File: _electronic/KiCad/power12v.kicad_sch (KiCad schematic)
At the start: 14 parts

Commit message: external flashing header
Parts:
- J_POW1: footprint Connector_BarrelJack:BarrelJack_GCT_DCJ200-10-A_Horizontal -> SnapEDA Library:BarrelJack_GCT_DCJ200-10-A_Horizontal
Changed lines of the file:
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@@
       (effects (font (size 1.27 1.27)) hide)
     )
-    (property "Footprint" "Connector_BarrelJack:BarrelJack_GCT_DCJ200-10-A_Horizontal" (id 2) (at 90.17 89.916 0)
+    (property "Footprint" "SnapEDA Library:BarrelJack_GCT_DCJ200-10-A_Horizontal" (id 2) (at 90.17 89.916 0)
       (effects (font (size 1.27 1.27)) hide)
     )

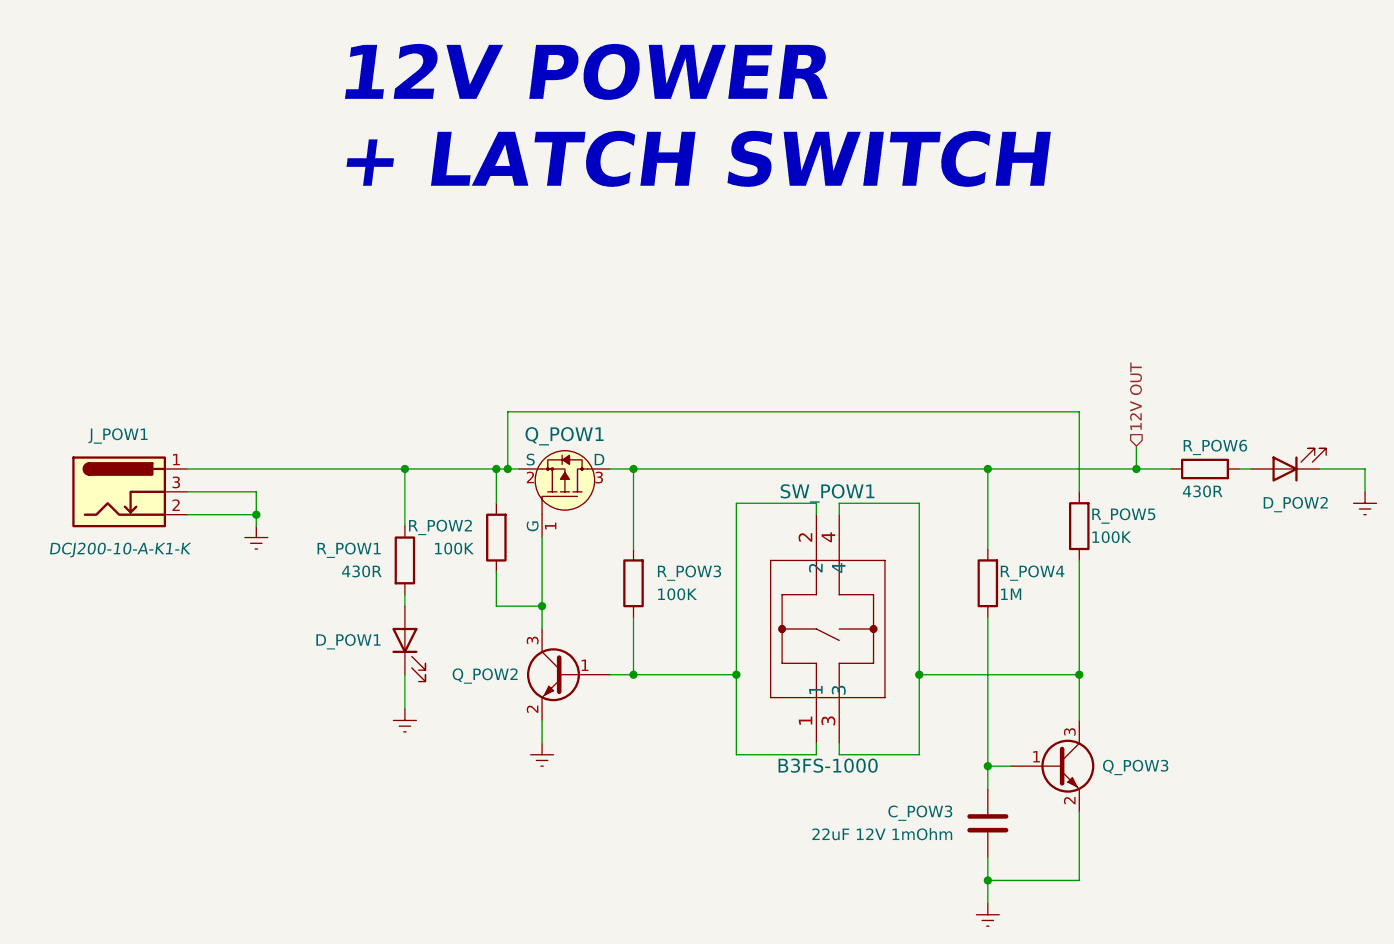
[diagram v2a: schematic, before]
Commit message: 6v and power latch backup
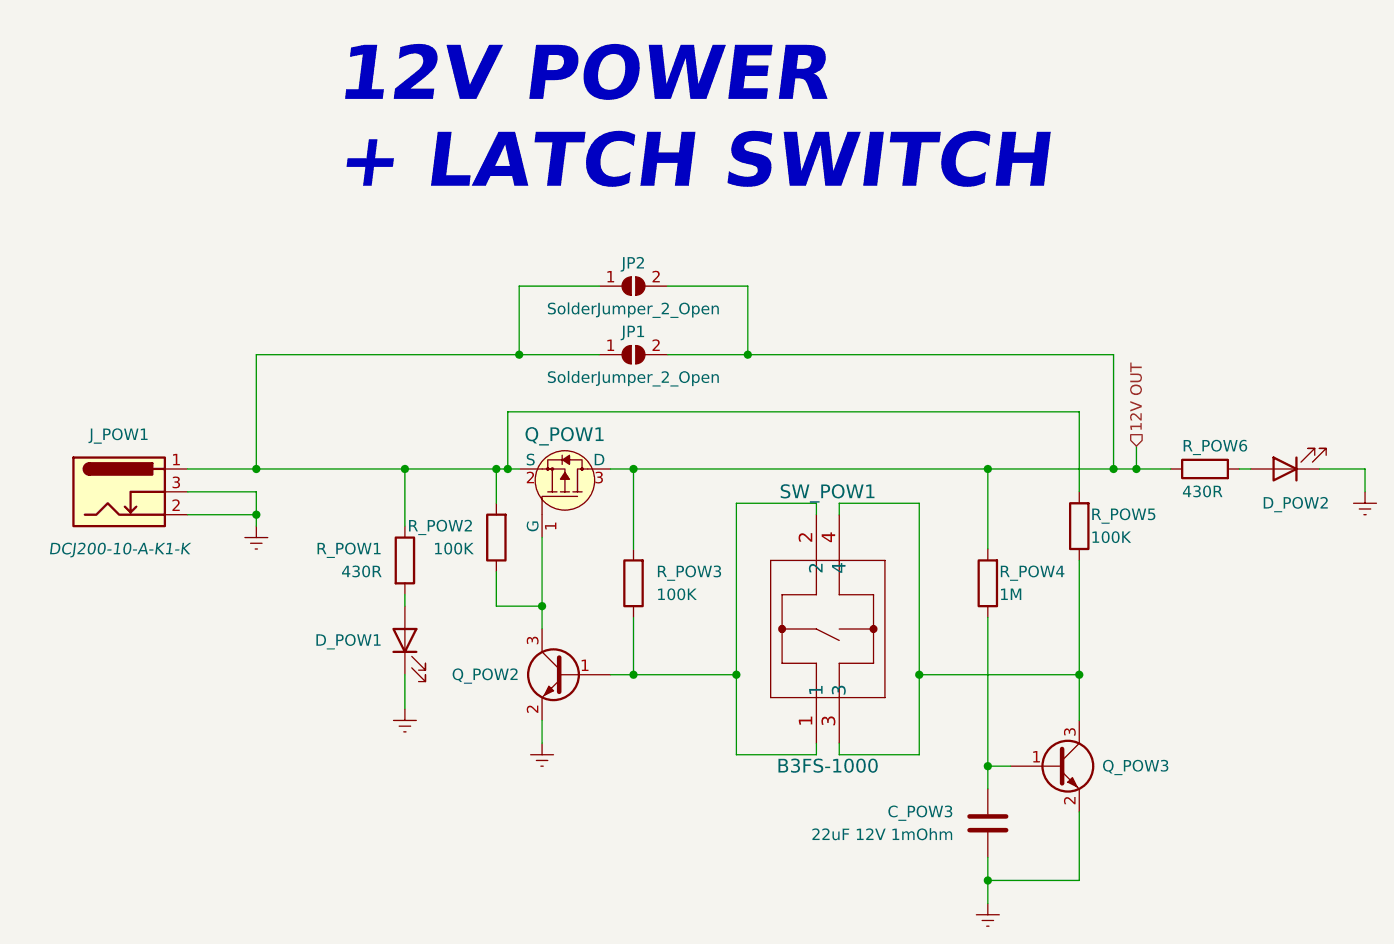
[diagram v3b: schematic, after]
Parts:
- added JP1, JP2: SolderJumper_2_Open, Jumper:SolderJumper-2_P1.3mm_Open_Pad1.0x1.5mm, symbol Jumper:SolderJumper_2_Open
- Q_POW1: value IRLML6302TRPBF -> SQ2351ES-T1_GE3; # IRLML6302TRPBF -> SQ2351ES-T1_GE3; Obs wes SI2303CDS-T1-BE3 ?? Id - Continuous Drain Current -> (none)
- Q_POW2, Q_POW3: Obs wes -> (none)
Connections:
- net 12V OUT: now also JP1.2 (B), JP2.2 (B)
- net at J_POW1.1, Q_POW1.2 (S), R_POW1.1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: now also JP1.1 (A), JP2.1 (A)
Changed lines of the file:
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@@
   (junction (at 201.93 86.36) (diameter 0) (color 0 0 0 0)
   )
+  (junction (at 158.75 73.66) (diameter 0) (color 0 0 0 0)
+  )
   (junction (at 130.81 86.36) (diameter 0) (color 0 0 0 0)
   )
+  (junction (at 104.14 86.36) (diameter 0) (color 0 0 0 0)
+  )
   (junction (at 120.65 86.36) (diameter 0) (color 0 0 0 0)
   )
@@
   (junction (at 195.58 109.22) (diameter 0) (color 0 0 0 0)
   )
+  (junction (at 199.39 86.36) (diameter 0) (color 0 0 0 0)
+  )
   (junction (at 132.08 86.36) (diameter 0) (color 0 0 0 0)
   )
@@
   (junction (at 185.42 132.08) (diameter 0) (color 0 0 0 0)
   )
+  (junction (at 133.35 73.66) (diameter 0) (color 0 0 0 0)
+  )
   (junction (at 185.42 86.36) (diameter 0) (color 0 0 0 0)
   )
@@
     (stroke (width 0) (type default) (color 0 0 0 0))
   )
+  (wire (pts (xy 158.75 66.04) (xy 158.75 73.66))
+    (stroke (width 0) (type default) (color 0 0 0 0))
+  )
+  (wire (pts (xy 158.75 73.66) (xy 199.39 73.66))
+    (stroke (width 0) (type default) (color 0 0 0 0))
+  )
+  (wire (pts (xy 104.14 86.36) (xy 120.65 86.36))
+    (stroke (width 0) (type default) (color 0 0 0 0))
+  )
   (wire (pts (xy 130.81 86.36) (xy 132.08 86.36))
     (stroke (width 0) (type default) (color 0 0 0 0))
@@
     (stroke (width 0) (type default) (color 0 0 0 0))
   )
+  (wire (pts (xy 149.86 66.04) (xy 158.75 66.04))
+    (stroke (width 0) (type default) (color 0 0 0 0))
+  )
   (wire (pts (xy 143.51 86.36) (xy 146.05 86.36))
     (stroke (width 0) (type default) (color 0 0 0 0))
@@
     (stroke (width 0) (type default) (color 0 0 0 0))
   )
+  (wire (pts (xy 149.86 73.66) (xy 158.75 73.66))
+    (stroke (width 0) (type default) (color 0 0 0 0))
+  )
   (wire (pts (xy 135.89 116.84) (xy 135.89 114.3))
     (stroke (width 0) (type default) (color 0 0 0 0))
@@
     (stroke (width 0) (type default) (color 0 0 0 0))
   )
+  (wire (pts (xy 199.39 86.36) (xy 201.93 86.36))
+    (stroke (width 0) (type default) (color 0 0 0 0))
+  )
   (wire (pts (xy 135.89 101.6) (xy 135.89 104.14))
     (stroke (width 0) (type default) (color 0 0 0 0))
@@
     (stroke (width 0) (type default) (color 0 0 0 0))
   )
+  (wire (pts (xy 133.35 73.66) (xy 104.14 73.66))
+    (stroke (width 0) (type default) (color 0 0 0 0))
+  )
   (wire (pts (xy 185.42 129.54) (xy 185.42 132.08))
     (stroke (width 0) (type default) (color 0 0 0 0))
@@
     (stroke (width 0) (type default) (color 0 0 0 0))
   )
+  (wire (pts (xy 104.14 73.66) (xy 104.14 86.36))
+    (stroke (width 0) (type default) (color 0 0 0 0))
+  )
   (wire (pts (xy 135.89 93.98) (xy 135.89 101.6))
     (stroke (width 0) (type default) (color 0 0 0 0))
@@
     (stroke (width 0) (type default) (color 0 0 0 0))
   )
-  (wire (pts (xy 185.42 86.36) (xy 201.93 86.36))
+  (wire (pts (xy 185.42 86.36) (xy 199.39 86.36))
+    (stroke (width 0) (type default) (color 0 0 0 0))
+  )
+  (wire (pts (xy 142.24 66.04) (xy 133.35 66.04))
     (stroke (width 0) (type default) (color 0 0 0 0))
   )
@@
     (stroke (width 0) (type default) (color 0 0 0 0))
   )
+  (wire (pts (xy 142.24 73.66) (xy 133.35 73.66))
+    (stroke (width 0) (type default) (color 0 0 0 0))
+  )
   (wire (pts (xy 104.14 91.44) (xy 104.14 92.71))
     (stroke (width 0) (type default) (color 0 0 0 0))
   )
+  (wire (pts (xy 199.39 73.66) (xy 199.39 86.36))
+    (stroke (width 0) (type default) (color 0 0 0 0))
+  )
   (wire (pts (xy 132.08 80.01) (xy 132.08 86.36))
     (stroke (width 0) (type default) (color 0 0 0 0))
@@
     (stroke (width 0) (type default) (color 0 0 0 0))
   )
-  (wire (pts (xy 96.52 86.36) (xy 120.65 86.36))
+  (wire (pts (xy 96.52 86.36) (xy 104.14 86.36))
     (stroke (width 0) (type default) (color 0 0 0 0))
   )
   (wire (pts (xy 195.58 80.01) (xy 132.08 80.01))
+    (stroke (width 0) (type default) (color 0 0 0 0))
+  )
+  (wire (pts (xy 133.35 66.04) (xy 133.35 73.66))
     (stroke (width 0) (type default) (color 0 0 0 0))
   )
@@
       (effects (font (size 1.27 1.27)) hide)
     )
-    (property "Obs" "wes" (id 8) (at 193.04 119.38 0)
+    (property "Obs" "" (id 8) (at 193.04 119.38 0)
       (effects (font (size 1.27 1.27)) hide)
     )
@@
     )
     (property "Mouser" "OK" (id 8) (at 185.42 125.73 0)
+      (effects (font (size 1.27 1.27)) hide)
+    )
+    (pin "1")
+    (pin "2")
+  )
+  (symbol (lib_id "Jumper:SolderJumper_2_Open") (at 146.05 66.04 0) (unit 1)
+    (in_bom yes) (on_board yes)
+    (property "Reference" "JP2" (id 0) (at 146.05 63.5 0))
+    (property "Value" "SolderJumper_2_Open" (id 1) (at 146.05 68.58 0))
+    (property "Footprint" "Jumper:SolderJumper-2_P1.3mm_Open_Pad1.0x1.5mm" (id 2) (at 146.05 66.04 0)
+      (effects (font (size 1.27 1.27)) hide)
+    )
+    (property "Datasheet" "~" (id 3) (at 146.05 66.04 0)
       (effects (font (size 1.27 1.27)) hide)
     )
@@
       (effects (font (size 1.524 1.524)))
     )
-    (property "Value" "IRLML6302TRPBF" (id 1) (at 138.43 82.55 90)
+    (property "Value" "SQ2351ES-T1_GE3" (id 1) (at 138.43 82.55 90)
       (effects (font (size 1.524 1.524)) hide)
     )
@@
       (effects (font (size 1.524 1.524)) (justify left) hide)
     )
-    (property "Datasheet" "https://br.mouser.com/datasheet/2/196/Infineon_IRLML6302_DataSheet_v01_01_EN-1732826.pdf" (id 3) (at 146.05 81.28 0)
+    (property "Datasheet" "https://br.mouser.com/datasheet/2/427/sq2351es-1764982.pdf" (id 3) (at 146.05 81.28 0)
       (effects (font (size 1.524 1.524)) (justify left) hide)
     )
-    (property "#" "IRLML6302TRPBF" (id 14) (at 138.43 86.36 90)
-      (effects (font (size 1.27 1.27)) hide)
-    )
-    (property "Description" "MOSFET P-CH 30V 4A SOT23" (id 13) (at 138.43 86.36 90)
+    (property "#" "SQ2351ES-T1_GE3" (id 14) (at 138.43 86.36 90)
+      (effects (font (size 1.27 1.27)) hide)
+    )
+    (property "Description" "MOSFET P-CH 20V 3.2A SOT23-3" (id 13) (at 138.43 86.36 90)
       (effects (font (size 1.27 1.27)) hide)
     )
@@
       (effects (font (size 1.27 1.27)) hide)
     )
-    (property "Obs" "wes SI2303CDS-T1-BE3 ??  Id - Continuous Drain Current" (id 17) (at 138.43 86.36 0)
+    (property "Obs" "" (id 17) (at 138.43 86.36 0)
       (effects (font (size 1.27 1.27)) hide)
     )
@@
     (pin "2")
   )
+  (symbol (lib_id "Jumper:SolderJumper_2_Open") (at 146.05 73.66 0) (unit 1)
+    (in_bom yes) (on_board yes)
+    (property "Reference" "JP1" (id 0) (at 146.05 71.12 0))
+    (property "Value" "SolderJumper_2_Open" (id 1) (at 146.05 76.2 0))
+    (property "Footprint" "Jumper:SolderJumper-2_P1.3mm_Open_Pad1.0x1.5mm" (id 2) (at 146.05 73.66 0)
+      (effects (font (size 1.27 1.27)) hide)
+    )
+    (property "Datasheet" "~" (id 3) (at 146.05 73.66 0)
+      (effects (font (size 1.27 1.27)) hide)
+    )
+    (pin "1")
+    (pin "2")
+  )
   (symbol (lib_id "Device:R") (at 146.05 99.06 180) (unit 1)
     (in_bom yes) (on_board yes)
@@
       (effects (font (size 1.27 1.27)) hide)
     )
-    (property "Obs" "wes" (id 8) (at 138.43 109.22 0)
-      (effects (font (size 1.27 1.27)) hide)
-    )
+    (property "Obs" "" (id 8) (at 138.43 109.22 0)
+      (effects (font (size 1.27 1.27)) hide)
+    )

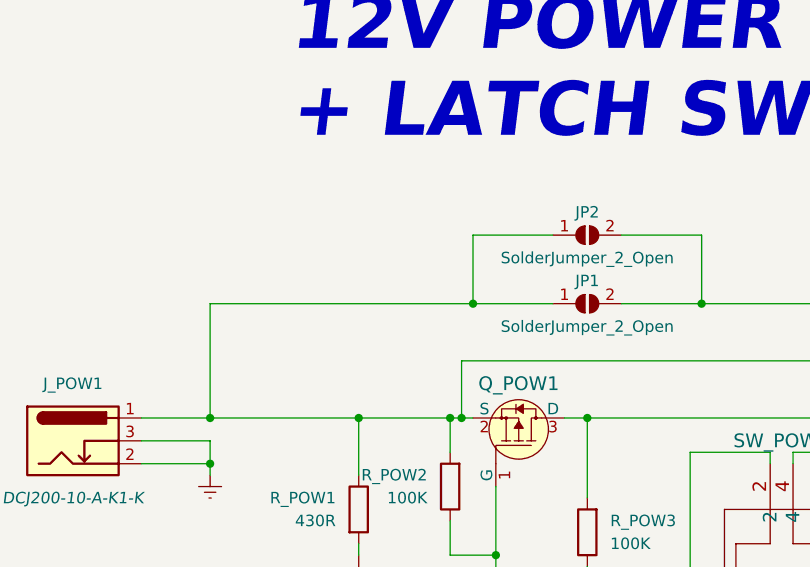
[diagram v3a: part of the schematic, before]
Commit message: revised IC packages, pins and footprints
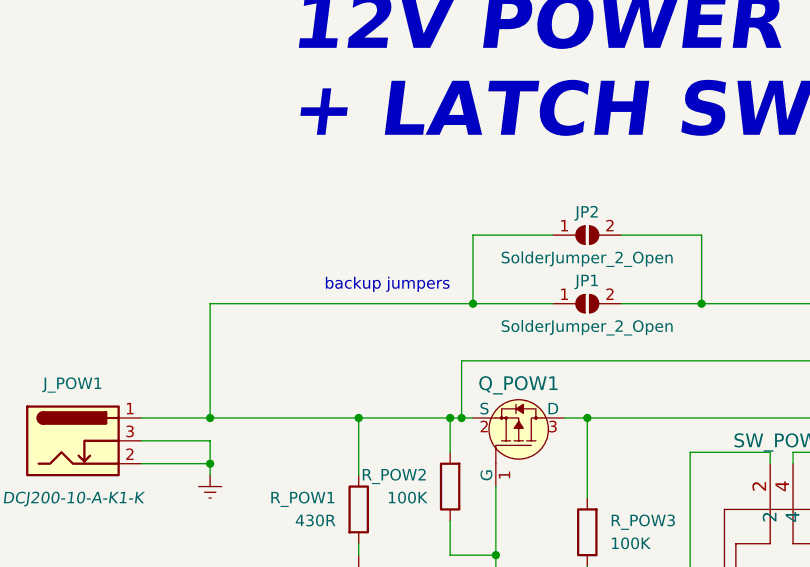
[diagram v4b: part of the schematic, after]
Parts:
- Q_POW1, Q_POW2, Q_POW3: footprint Package_TO_SOT_SMD:SOT-23 -> Package_TO_SOT_SMD:SOT-23_Handsoldering
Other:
- note added: "backup jumpers"
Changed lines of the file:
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@@
     (stroke (width 0) (type default) (color 0 0 0 0))
+  )
+  (text "backup jumpers" (at 116.84 72.39 0)
+    (effects (font (size 1.27 1.27)) (justify left bottom))
   )
   (text "12V POWER\n+ LATCH SWITCH" (at 113.03 55.88 0)
@@
       (effects (font (size 1.27 1.27)) (justify left) hide)
     )
-    (property "Footprint" "Package_TO_SOT_SMD:SOT-23" (id 2) (at 198.12 121.285 0)
+    (property "Footprint" "Package_TO_SOT_SMD:SOT-23_Handsoldering" (id 2) (at 198.12 121.285 0)
       (effects (font (size 1.27 1.27) italic) (justify left) hide)
     )
@@
       (effects (font (size 1.524 1.524)) hide)
     )
-    (property "Footprint" "Package_TO_SOT_SMD:SOT-23" (id 2) (at 143.51 81.28 0)
+    (property "Footprint" "Package_TO_SOT_SMD:SOT-23_Handsoldering" (id 2) (at 143.51 81.28 0)
       (effects (font (size 1.524 1.524)) (justify left) hide)
     )
@@
       (effects (font (size 1.27 1.27)) (justify left) hide)
     )
-    (property "Footprint" "Package_TO_SOT_SMD:SOT-23" (id 2) (at 133.35 111.125 0)
-      (effects (font (size 1.27 1.27) italic) (justify left) hide)
-    )
+    (property "Footprint" "Package_TO_SOT_SMD:SOT-23_Handsoldering" (id 2) (at 133.35 111.125 0)
+      (effects (font (size 1.27 1.27) italic) (justify left) hide)
+    )

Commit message: schematics footer and export
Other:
- company: (none) -> Andrei Speridiao
- title: (none) -> E-TKT
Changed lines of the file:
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@@
 (kicad_sch (version 20211123) (generator eeschema)
   (paper "A4")
+  (title_block
+    (title "E-TKT")
+    (date "2022-07-21")
+    (rev "3")
+    (company "Andrei Speridiao")
+  )
   (junction (at 201.93 86.36) (diameter 0) (color 0 0 0 0)
   )
